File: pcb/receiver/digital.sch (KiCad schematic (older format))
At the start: 55 parts, among them J301 Conn_01x03, J302 Conn_01x04, J303 Conn_01x03, J304 USB_B_Micro, U301 ATTINY412-SSNR, U302 STM32F070F6P6, U303 MAX11666AUB+T, U304 L78L33ABUTR, Y301 ABM3B-8.000MHZ-10-1UT

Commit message: Finish footprinting/sourcing all components
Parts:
- D301, D303: Mouser (none) -> 583-2SS100L-W
- D302: footprint (none) -> receiver-footprints:Rectron_SOD-123FL
- D305, D306: footprint (none) -> receiver-footprints:TI_X1SON; Mouser (none) -> 595-TPD1E04U04DPYR
- J301: value Conn_01x03 -> UART; footprint (none) -> Socket_Strips:Socket_Strip_Straight_1x03_Pitch2.54mm; Mouser (none) -> NoPart
- J302: value Conn_01x04 -> STM32_SWD; footprint (none) -> Socket_Strips:Socket_Strip_Straight_2x02_Pitch2.54mm; Mouser (none) -> NoPart
- J303: value Conn_01x03 -> AVR_DEBUG; footprint (none) -> Socket_Strips:Socket_Strip_Straight_1x03_Pitch2.54mm; Mouser (none) -> NoPart
- J304: footprint (none) -> receiver-footprints:Amphenol_10118194; Mouser (none) -> 649-10118194-0001LF
- R302, R305: footprint (none) -> Resistors_SMD:R_0603_HandSoldering; Mouser (none) -> 755-SFR03EZPJ000
- R311: footprint (none) -> Resistors_SMD:R_0402; Mouser (none) -> 603-RC0402JR-13100KL
- R315, R316: footprint (none) -> Resistors_SMD:R_0402; Mouser (none) -> 603-RC0402JR-7D330RL
- R318: footprint (none) -> Resistors_SMD:R_0603_HandSoldering; Mouser (none) -> 603-RC0603FR-0710KL
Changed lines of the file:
@@
 F 0 "R302" H 1980 3070 50  0000 L CNN
 F 1 "0" H 1980 3010 50  0000 L CNN
-F 2 "" H 1950 3050 50  0001 C CNN
+F 2 "Resistors_SMD:R_0603_HandSoldering" H 1950 3050 50  0001 C CNN
 F 3 "~" H 1950 3050 50  0001 C CNN
+F 4 "755-SFR03EZPJ000" H 1950 3050 50  0001 C CNN "Mouser"
 	1    1950 3050
 	0    -1   -1   0
@@
 F 0 "R305" H 1980 3570 50  0000 L CNN
 F 1 "0" H 1980 3510 50  0000 L CNN
-F 2 "" H 1950 3550 50  0001 C CNN
+F 2 "Resistors_SMD:R_0603_HandSoldering" H 1950 3550 50  0001 C CNN
 F 3 "~" H 1950 3550 50  0001 C CNN
+F 4 "755-SFR03EZPJ000" H 1950 3550 50  0001 C CNN "Mouser"
 	1    1950 3550
 	0    -1   1    0
@@
 Wire Wire Line
 	8450 1800 8350 1800
-Text HLabel 10150 2700 2    50   Input ~ 0
-ANALOG_EN
 Wire Wire Line
 	9100 1700 9100 1850
@@
 F 0 "R311" H 7580 4570 50  0000 L CNN
 F 1 "100k" H 7580 4510 50  0000 L CNN
-F 2 "" H 7550 4550 50  0001 C CNN
+F 2 "Resistors_SMD:R_0402" H 7550 4550 50  0001 C CNN
 F 3 "~" H 7550 4550 50  0001 C CNN
+F 4 "603-RC0402JR-13100KL" H 7550 4550 50  0001 C CNN "Mouser"
 	1    7550 4550
 	1    0    0    -1
@@
 F 0 "D302" H 4700 3080 50  0000 L CNN
 F 1 "2SS100L-W" H 4470 2920 50  0000 L CNN
-F 2 "" V 4750 3000 50  0001 C CNN
+F 2 "receiver-footprints:Rectron_SOD-123FL" V 4750 3000 50  0001 C CNN
 F 3 "~" V 4750 3000 50  0001 C CNN
 F 4 "583-2SS100L-W" H 4750 3000 50  0001 C CNN "Mouser"
@@
 F 2 "receiver-footprints:Rectron_SOD-123FL" V 4750 3600 50  0001 C CNN
 F 3 "~" V 4750 3600 50  0001 C CNN
+F 4 "583-2SS100L-W" V 4750 3600 50  0001 C CNN "Mouser"
 	1    4750 3600
 	0    1    1    0
@@
 P 10900 4600
 F 0 "J303" H 10900 4800 50  0000 C CNN
-F 1 "Conn_01x03" H 10900 4400 50  0000 C CNN
-F 2 "" H 10900 4600 50  0001 C CNN
+F 1 "AVR_DEBUG" H 10900 4400 50  0000 C CNN
+F 2 "Socket_Strips:Socket_Strip_Straight_1x03_Pitch2.54mm" H 10900 4600 50  0001 C CNN
 F 3 "~" H 10900 4600 50  0001 C CNN
+F 4 "NoPart" H 10900 4600 50  0001 C CNN "Mouser"
 	1    10900 4600
 	1    0    0    -1
@@
 P 10900 5200
 F 0 "J301" H 10900 5400 50  0000 C CNN
-F 1 "Conn_01x03" H 10900 5000 50  0000 C CNN
-F 2 "" H 10900 5200 50  0001 C CNN
+F 1 "UART" H 10900 5000 50  0000 C CNN
+F 2 "Socket_Strips:Socket_Strip_Straight_1x03_Pitch2.54mm" H 10900 5200 50  0001 C CNN
 F 3 "~" H 10900 5200 50  0001 C CNN
+F 4 "NoPart" H 10900 5200 50  0001 C CNN "Mouser"
 	1    10900 5200
 	1    0    0    -1
@@
 P 10900 5950
 F 0 "J302" H 10900 6150 50  0000 C CNN
-F 1 "Conn_01x04" H 10900 5650 50  0000 C CNN
-F 2 "" H 10900 5950 50  0001 C CNN
+F 1 "STM32_SWD" H 10900 5650 50  0000 C CNN
+F 2 "Socket_Strips:Socket_Strip_Straight_2x02_Pitch2.54mm" H 10900 5950 50  0001 C CNN
 F 3 "~" H 10900 5950 50  0001 C CNN
+F 4 "NoPart" H 10900 5950 50  0001 C CNN "Mouser"
 	1    10900 5950
 	1    0    0    -1
@@
 F 0 "R315" H 10530 5320 50  0000 L CNN
 F 1 "330" H 10530 5260 50  0000 L CNN
-F 2 "" H 10500 5300 50  0001 C CNN
+F 2 "Resistors_SMD:R_0402" H 10500 5300 50  0001 C CNN
 F 3 "~" H 10500 5300 50  0001 C CNN
+F 4 "603-RC0402JR-7D330RL" H 10500 5300 50  0001 C CNN "Mouser"
 	1    10500 5300
 	0    -1   1    0
@@
 F 0 "R316" H 10380 4620 50  0000 L CNN
 F 1 "330" H 10380 4560 50  0000 L CNN
-F 2 "" H 10350 4600 50  0001 C CNN
+F 2 "Resistors_SMD:R_0402" H 10350 4600 50  0001 C CNN
 F 3 "~" H 10350 4600 50  0001 C CNN
+F 4 "603-RC0402JR-7D330RL" H 10350 4600 50  0001 C CNN "Mouser"
 	1    10350 4600
 	0    -1   -1   0
@@
 F 0 "J304" H 10550 3800 50  0000 L CNN
 F 1 "USB_B_Micro" H 10550 3700 50  0000 L CNN
-F 2 "" H 10900 3300 50  0001 C CNN
+F 2 "receiver-footprints:Amphenol_10118194" H 10900 3300 50  0001 C CNN
 F 3 "~" H 10900 3300 50  0001 C CNN
+F 4 "649-10118194-0001LF" H 10750 3350 50  0001 C CNN "Mouser"
 	1    10750 3350
 	-1   0    0    -1
@@
 F 0 "D305" H 9950 3730 50  0000 L CNN
 F 1 "TPD1E04U04DPYR" H 9850 3570 50  0000 L CNN
-F 2 "" V 10000 3650 50  0001 C CNN
+F 2 "receiver-footprints:TI_X1SON" V 10000 3650 50  0001 C CNN
 F 3 "~" V 10000 3650 50  0001 C CNN
+F 4 "595-TPD1E04U04DPYR" V 10000 3650 50  0001 C CNN "Mouser"
 	1    10000 3650
 	0    -1   1    0
@@
 F 0 "D306" H 10200 3730 50  0000 L CNN
 F 1 "TPD1E04U04DPYR" H 10100 3570 50  0000 L CNN
-F 2 "" V 10250 3650 50  0001 C CNN
+F 2 "receiver-footprints:TI_X1SON" V 10250 3650 50  0001 C CNN
 F 3 "~" V 10250 3650 50  0001 C CNN
+F 4 "595-TPD1E04U04DPYR" V 10250 3650 50  0001 C CNN "Mouser"
 	1    10250 3650
 	0    -1   1    0
@@
 F 0 "R318" H 2880 720 50  0000 L CNN
 F 1 "10k" H 2880 660 50  0000 L CNN
-F 2 "" H 2850 700 50  0001 C CNN
+F 2 "Resistors_SMD:R_0603_HandSoldering" H 2850 700 50  0001 C CNN
 F 3 "~" H 2850 700 50  0001 C CNN
+F 4 "603-RC0603FR-0710KL" H 2850 700 50  0001 C CNN "Mouser"
 	1    2850 700
 	0    -1   1    0
@@
 F 2 "receiver-footprints:Rectron_SOD-123FL" V 2150 5400 50  0001 C CNN
 F 3 "~" V 2150 5400 50  0001 C CNN
+F 4 "583-2SS100L-W" V 2150 5400 50  0001 C CNN "Mouser"
 	1    2150 5400
 	1    0    0    -1

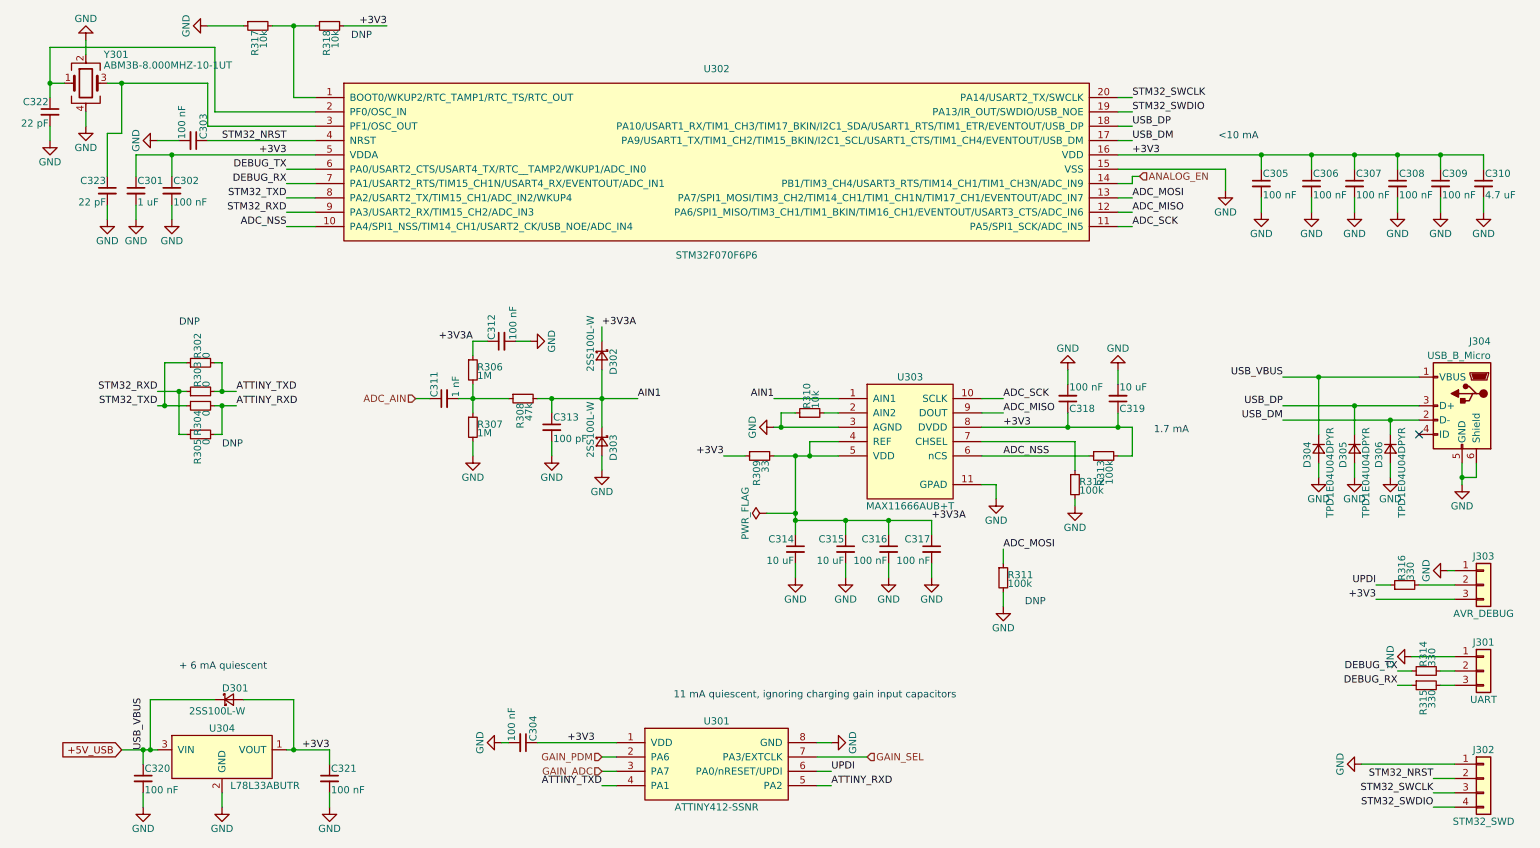
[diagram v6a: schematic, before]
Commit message: Most of the layout done TODO add test points for +12V, AVR_UART, various amplifier stage outputs
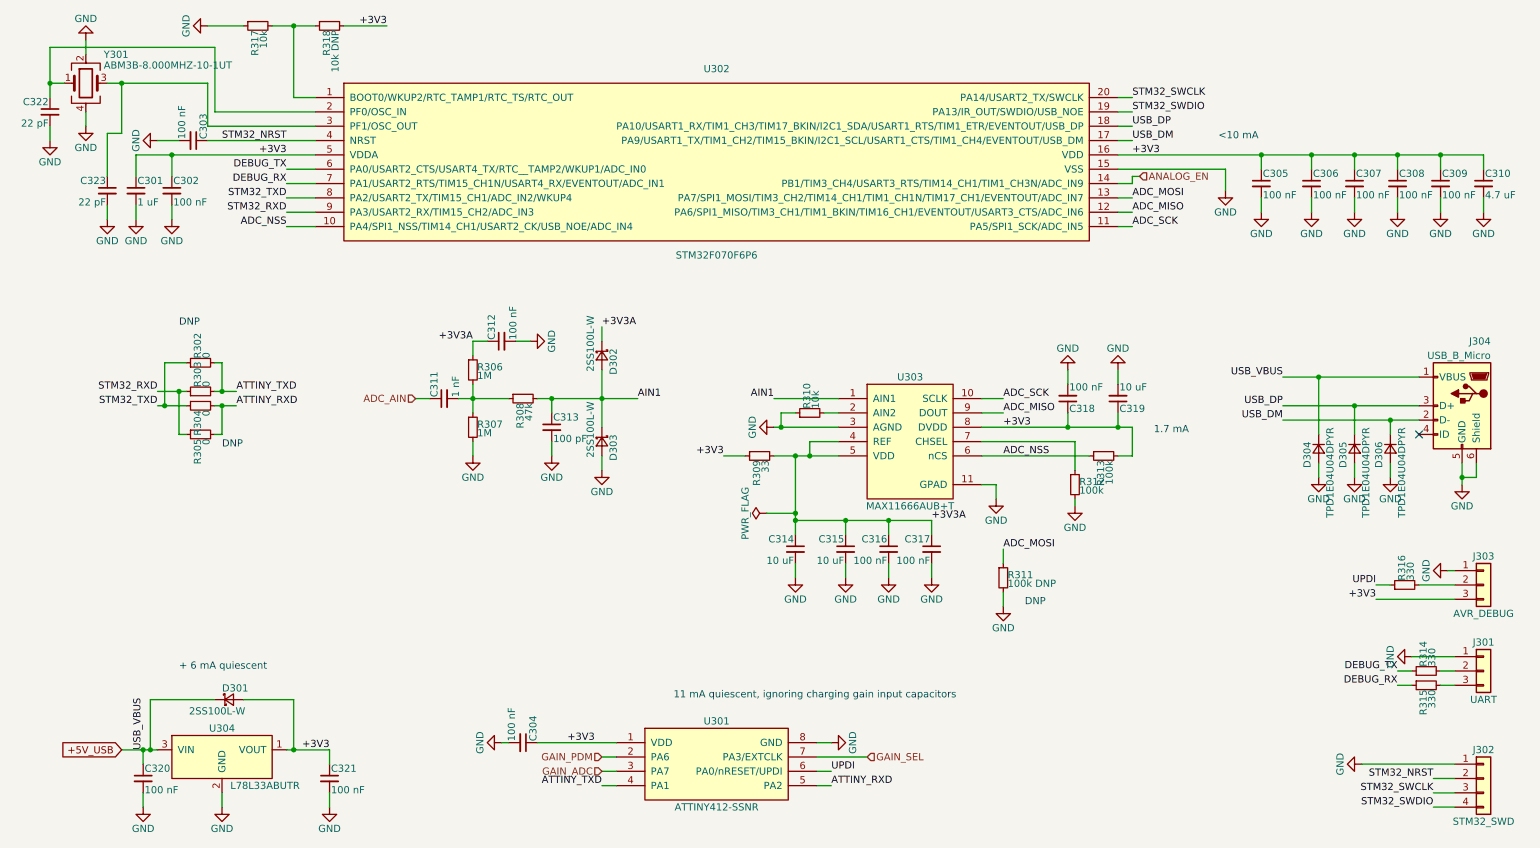
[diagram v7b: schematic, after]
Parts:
- R311: value 100k -> 100k DNP
- R318: value 10k -> 10k DNP
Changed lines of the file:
@@
 P 7550 4550
 F 0 "R311" H 7580 4570 50  0000 L CNN
-F 1 "100k" H 7580 4510 50  0000 L CNN
+F 1 "100k DNP" H 7580 4510 50  0000 L CNN
 F 2 "Resistors_SMD:R_0402" H 7550 4550 50  0001 C CNN
 F 3 "~" H 7550 4550 50  0001 C CNN
@@
 P 2850 700
 F 0 "R318" H 2880 720 50  0000 L CNN
-F 1 "10k" H 2880 660 50  0000 L CNN
+F 1 "10k DNP" H 2880 660 50  0000 L CNN
 F 2 "Resistors_SMD:R_0603_HandSoldering" H 2850 700 50  0001 C CNN
 F 3 "~" H 2850 700 50  0001 C CNN
@@
 Text Notes 7700 4750 0    50   ~ 0
 DNP
-Text Notes 3000 800  0    50   ~ 0
-DNP
-$Comp
+$Comp

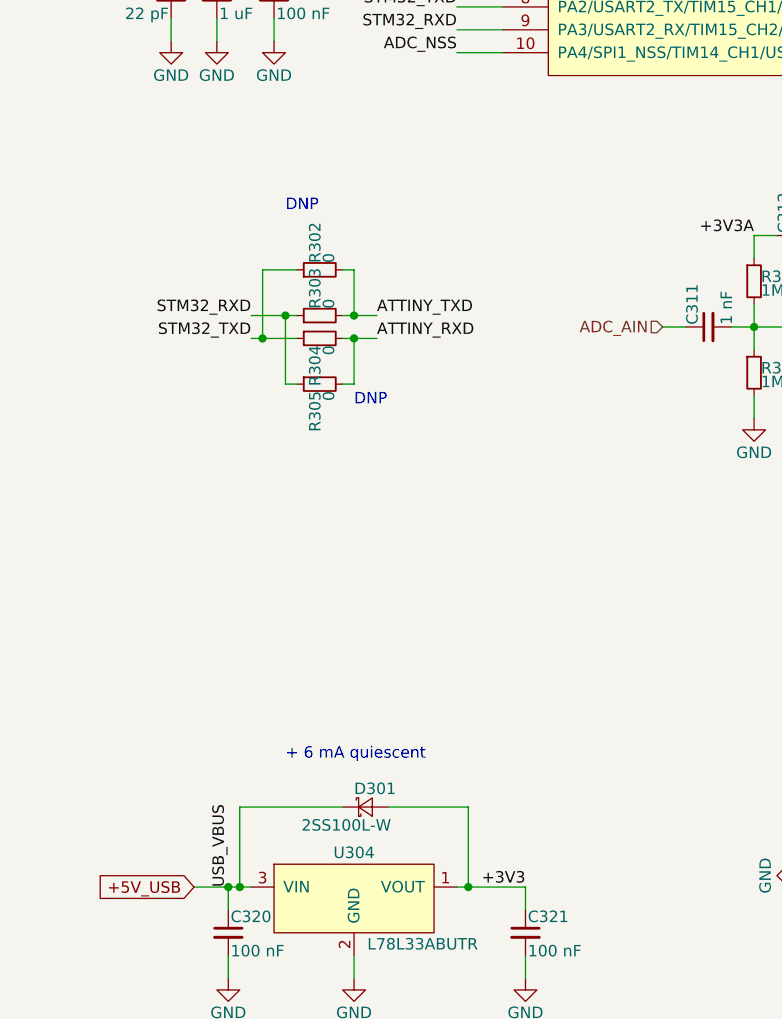
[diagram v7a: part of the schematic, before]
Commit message: Add copper fills and outline, autofill test point footprints, TODO finish placing test points and moving silkscreen
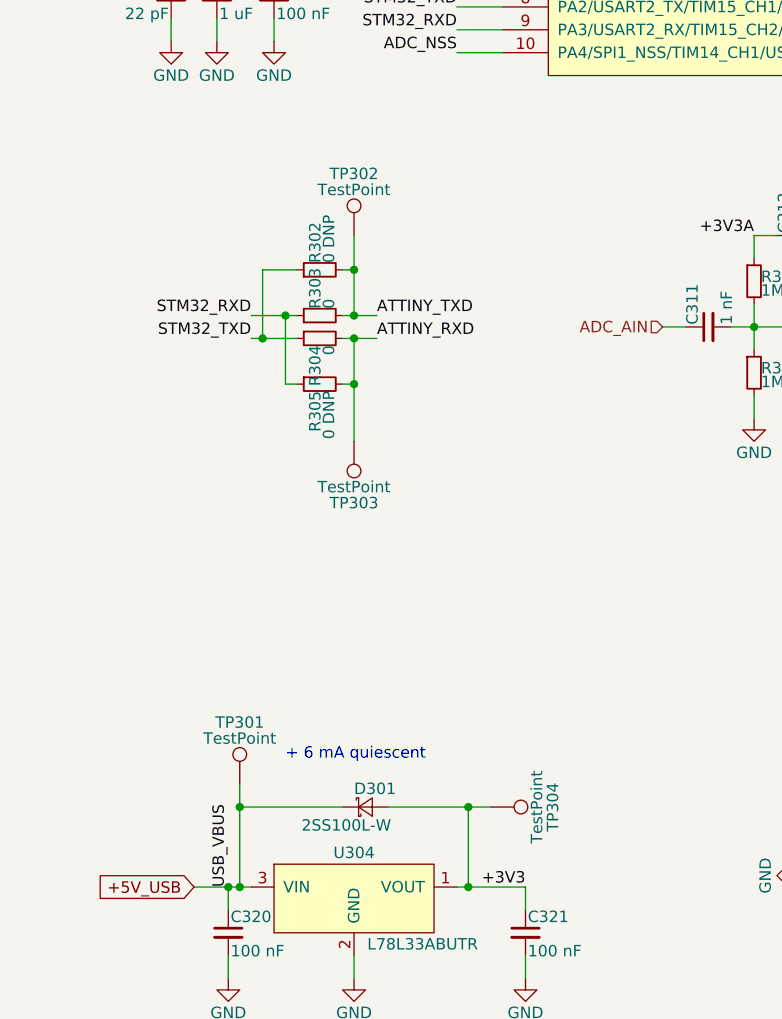
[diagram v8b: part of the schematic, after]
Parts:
- added TP301, TP302, TP303, TP304: TestPoint, Measurement_Points:Measurement_Point_Round-SMD-Pad_Small, symbol Connector:TestPoint
- R302, R305: value 0 -> 0 DNP
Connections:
- net +3V3: now also TP304.1
- net +5V_USB: now also TP301.1
- net ATTINY_RXD: now also TP303.1
- net ATTINY_TXD: now also TP302.1
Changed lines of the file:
@@
 P 1950 3050
 F 0 "R302" H 1980 3070 50  0000 L CNN
-F 1 "0" H 1980 3010 50  0000 L CNN
+F 1 "0 DNP" H 1980 3010 50  0000 L CNN
 F 2 "Resistors_SMD:R_0603_HandSoldering" H 1950 3050 50  0001 C CNN
 F 3 "~" H 1950 3050 50  0001 C CNN
@@
 P 1950 3550
 F 0 "R305" H 1980 3570 50  0000 L CNN
-F 1 "0" H 1980 3510 50  0000 L CNN
+F 1 "0 DNP" H 1980 3510 50  0000 L CNN
 F 2 "Resistors_SMD:R_0603_HandSoldering" H 1950 3550 50  0001 C CNN
 F 3 "~" H 1950 3550 50  0001 C CNN
@@
 Wire Wire Line
 	2100 6050 2100 6150
-Text Notes 1800 2800 0    50   ~ 0
-DNP
-Text Notes 2100 3650 0    50   ~ 0
-DNP
 Text Notes 7700 4750 0    50   ~ 0
 DNP
@@
 Wire Wire Line
 	4300 5700 4850 5700
+$Comp
+L Connector:TestPoint TP304
+U 1 1 5C2C1BD7
+P 2700 5400
+F 0 "TP304" H 2700 5670 50  0000 C CNN
+F 1 "TestPoint" H 2700 5600 50  0000 C CNN
+F 2 "Measurement_Points:Measurement_Point_Round-SMD-Pad_Small" H 2900 5400 50  0001 C CNN
+F 3 "~" H 2900 5400 50  0001 C CNN
+F 4 "NoPart" H 2900 5400 50  0001 C CNN "Mouser"
+	1    2700 5400
+	0    1    1    0
+$EndComp
+Wire Wire Line
+	2700 5400 2600 5400
+Connection ~ 2600 5400
+$Comp
+L Connector:TestPoint TP301
+U 1 1 5C2CDF5E
+P 1600 5300
+F 0 "TP301" H 1600 5570 50  0000 C CNN
+F 1 "TestPoint" H 1600 5500 50  0000 C CNN
+F 2 "Measurement_Points:Measurement_Point_Round-SMD-Pad_Small" H 1800 5300 50  0001 C CNN
+F 3 "~" H 1800 5300 50  0001 C CNN
+F 4 "NoPart" H 1800 5300 50  0001 C CNN "Mouser"
+	1    1600 5300
+	1    0    0    -1
+$EndComp
+Wire Wire Line
+	1600 5300 1600 5400
+Connection ~ 1600 5400
+$Comp
+L Connector:TestPoint TP302
+U 1 1 5C2D99F9
+P 2100 2900
+F 0 "TP302" H 2100 3170 50  0000 C CNN
+F 1 "TestPoint" H 2100 3100 50  0000 C CNN
+F 2 "Measurement_Points:Measurement_Point_Round-SMD-Pad_Small" H 2300 2900 50  0001 C CNN
+F 3 "~" H 2300 2900 50  0001 C CNN
+F 4 "NoPart" H 2300 2900 50  0001 C CNN "Mouser"
+	1    2100 2900
+	1    0    0    -1
+$EndComp
+Wire Wire Line
+	2100 2900 2100 3050
+Connection ~ 2100 3050
+$Comp
+L Connector:TestPoint TP303
+U 1 1 5C2E5AD2
+P 2100 3800
+F 0 "TP303" H 2100 4070 50  0000 C CNN
+F 1 "TestPoint" H 2100 4000 50  0000 C CNN
+F 2 "Measurement_Points:Measurement_Point_Round-SMD-Pad_Small" H 2300 3800 50  0001 C CNN
+F 3 "~" H 2300 3800 50  0001 C CNN
+F 4 "NoPart" H 2300 3800 50  0001 C CNN "Mouser"
+	1    2100 3800
+	-1   0    0    1
+$EndComp
+Wire Wire Line
+	2100 3800 2100 3550
+Connection ~ 2100 3550
 $EndSCHEMATC
